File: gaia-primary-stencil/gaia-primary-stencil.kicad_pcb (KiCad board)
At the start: 2 copper layers, 100 x 100 mm, 103 parts, among them IC2 ADXL375BCCZ, J2 Conn_01x05_Socket, J3 USB_A, U1 CH340N, U12 ICM-20948, U13 ICM-20948, U2 AP2112K-3.3, U3 switch, U4 STM32F103C8Tx, U5 MAX31865xTP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

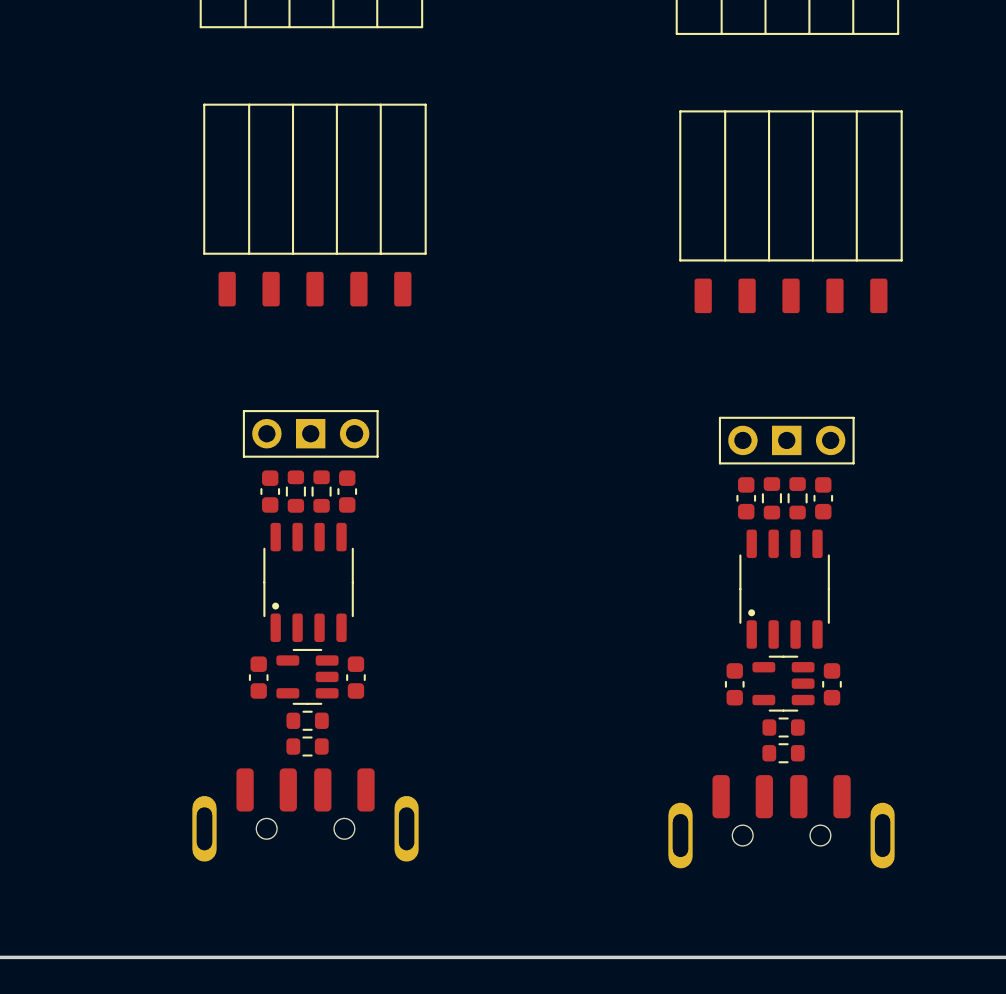
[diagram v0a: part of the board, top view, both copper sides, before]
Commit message: adding camera bott to stencil
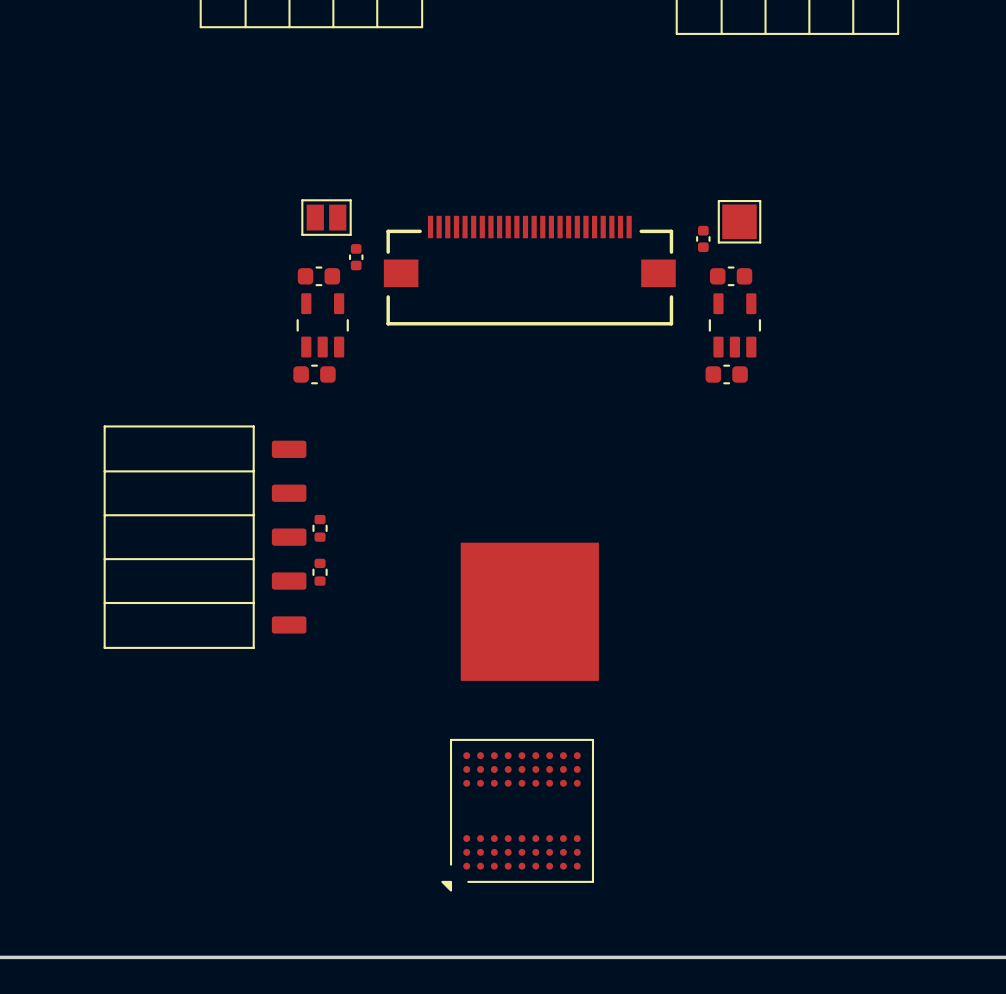
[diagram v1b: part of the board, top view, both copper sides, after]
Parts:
- removed the C1 at (141.2, 138.7)
- removed the C1 at (113.7, 138.3)
- removed the C2 at (145.7, 138.7)
- removed the C2 at (118.2, 138.3)
- removed the C3 at (146.2, 149.5)
- removed the C3 at (118.7, 149.1)
- removed the C4 at (113.0, 149.1)
- removed the C4 at (140.6, 149.5)
- removed the D1 at (143.4, 153.5)
- removed the D1 at (115.8, 153.1)
- removed the J2 at (148.9, 126.4)
- removed the J2 at (121.4, 126.0)
- removed the J3 at (115.7, 166.2)
- removed the J3 at (143.3, 166.6)
- removed the R1 at (116.7, 138.3)
- removed the R1 at (144.2, 138.7)
- removed the R2 at (142.7, 138.7)
- removed the R2 at (115.2, 138.3)
- removed the R3 at (115.9, 151.6)
- removed the R3 at (143.4, 152.0)
- removed the U1 at (115.9, 143.6)
- removed the U1 at (143.5, 144.0)
- removed the U2 at (143.4, 149.5)
- removed the U2 at (115.8, 149.1)
- removed the U3 at (141.1, 135.4)
- removed the U3 at (113.5, 135.0)
- added C38: 1uF, Capacitor_SMD:C_0603_1608Metric, F.Cu at (140.4, 125.9)
- added C42: 100nF, Capacitor_SMD:C_0402_1005Metric, F.Cu at (118.7, 124.8)
- added C43: 100nF, Capacitor_SMD:C_0402_1005Metric, F.Cu at (138.8, 123.7)
- added C44: 1uF, Capacitor_SMD:C_0603_1608Metric, F.Cu at (116.5, 125.9)
- added C5: 1uF, Capacitor_SMD:C_0603_1608Metric, F.Cu at (140.1, 131.6)
- added C6: 1uF, Capacitor_SMD:C_0603_1608Metric, F.Cu at (116.3, 131.6)
- added IC1: W9825G6JB-6I, Package_BGA:Alliance_TFBGA-54_8x8mm_Layout9x9_P0.8mm, F.Cu at (128.3, 156.8)
- added IC2: TLV74315PDBVR, gaia-camera-footprints:TLV74315PDBVR, F.Cu at (116.7, 128.7)
- added J3: Conn_01x05_Socket, gaia-camera-footprints:PinSocket_1x05_P2.54mm_Horizontal, F.Cu at (114.2, 135.9)
- added J6: OV5640, gaia-camera-footprints:OV5640, F.Cu at (128.7, 125.8)
- added JP1: SolderJumper_2_Open, Jumper:SolderJumper-2_P1.3mm_Open_Pad1.0x1.5mm, F.Cu at (116.9, 122.5)
- added R12: 10k, Resistor_SMD:R_0402_1005Metric, F.Cu at (116.6, 143.0)
- added R13: 10k, Resistor_SMD:R_0402_1005Metric, F.Cu at (116.6, 140.5)
- added TP1: TestPoint, TestPoint:TestPoint_Pad_2.0x2.0mm, F.Cu at (140.9, 122.7)
- added U6: TLV74328PDBVR, gaia-camera-footprints:TLV74328PDBVR, F.Cu at (140.6, 128.7)
